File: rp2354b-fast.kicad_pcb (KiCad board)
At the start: 4 copper layers, 70 x 70 mm, 90 parts, among them J1 USB_C_Receptacle_USB2.0_16P, J2 TC2030-Tag, J3 Batt-Con, J4 MSD-10-C, J5 STPR_OUT, J6 Conn_01x03_Socket, SW1 BOOT, SW2 RUN, U1 RP2354B, U2 TPS63061, U3 USBLC6-2P6, U4 BMP581, U5 TLV75801PDRV, U6 TLV75533PDRV, U7 DRV8461SPWP, U8 ISM6HG256X, U9 MMC5983MA, Y1 12MHz

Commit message: v1.1c
sx1262 placement
need to route and assign pins
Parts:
- added C47: 100nF, Capacitor_SMD:C_0402_1005Metric, B.Cu at (127.5, 113.5)
- added C48: 10uF, Capacitor_SMD:C_0402_1005Metric, B.Cu at (125.6, 113.5)
- added U11: SX1262, WS-CORE-SX1262:CORE-1262, B.Cu at (118.4, 125.0)
- J4: value MSD-10-C -> CUI_MSD-10-C
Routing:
- net GND: track 56.5 -> 69.3 mm, vias 67 -> 73
- net +3V3: vias 35 -> 36

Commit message: sx1262 routes
routed!!
production ready??
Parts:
- J4: value CUI_MSD-10-C -> MSD-10-C
- moved R16 4.40 mm to (110.1, 104.4)
- moved R17 3.30 mm to (114.5, 104.4)
- moved R18 1.10 mm to (111.2, 104.4)
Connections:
- J4 pad 02: /GPIO14_CSN_SD -> /GPIO09_CSN_SD
- J4 pad 03: /GPIO19_SPI0_TX -> /GPIO11_SPI1_TX
- J4 pad 05: /GPIO18_SPI0_SCK -> /GPIO10_SPI1_SCK
- J4 pad 07: /GPIO16_SPI0_RX -> /GPIO08_SPI1_RX
- R15 pad 2: /GPIO16_SPI0_RX -> /GPIO08_SPI1_RX
- R16 pad 2: /GPIO18_SPI0_SCK -> /GPIO09_CSN_SD
- R17 pad 2: /GPIO19_SPI0_TX -> /GPIO10_SPI1_SCK
- R18 pad 2: /GPIO14_CSN_SD -> /GPIO11_SPI1_TX
- U1 pad 11: unconnected-(U1-GPIO12-Pad11) -> /GPIO12_CSN_RAD
- U1 pad 12: unconnected-(U1-GPIO13-Pad12) -> /GPIO13_DIO1_RAD
- U1 pad 13: unconnected-(U1-GPIO14-Pad13) -> /GPIO14_BUSY_RAD
- U1 pad 14: /GPIO14_CSN_SD -> /GPIO15_RESET_RAD
- U1 pad 6: unconnected-(U1-GPIO8-Pad6) -> /GPIO08_SPI1_RX
- U1 pad 7: unconnected-(U1-GPIO9-Pad7) -> /GPIO09_CSN_SD
- U1 pad 8: unconnected-(U1-GPIO10-Pad8) -> /GPIO10_SPI1_SCK
- U1 pad 9: unconnected-(U1-GPIO11-Pad9) -> /GPIO11_SPI1_TX
- U11 pad 14: unconnected-(U11-DIO1-Pad14) -> /GPIO13_DIO1_RAD
- U11 pad 3: unconnected-(U11-CS-Pad3) -> /GPIO12_CSN_RAD
- U11 pad 4: unconnected-(U11-CLK-Pad4) -> /GPIO10_SPI1_SCK
- U11 pad 5: unconnected-(U11-MOSI-Pad5) -> /GPIO11_SPI1_TX
- U11 pad 6: unconnected-(U11-MISO-Pad6) -> /GPIO08_SPI1_RX
- U11 pad 7: unconnected-(U11-RESET-Pad7) -> /GPIO15_RESET_RAD
- U11 pad 8: unconnected-(U11-BUSY-Pad8) -> /GPIO14_BUSY_RAD
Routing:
- net /GPIO10_SPI1_SCK: track 0.00 -> 70.0 mm, vias 0 -> 1
- net /GPIO08_SPI1_RX: track 0.00 -> 63.1 mm, vias 0 -> 1
- net /GPIO11_SPI1_TX: track 0.00 -> 58.7 mm, vias 0 -> 1
- net /GPIO12_CSN_RAD: track 0.00 -> 51.2 mm, vias 0 -> 1
- net /GPIO14_CSN_SD: track 48.2 -> 0.00 mm, vias 2 -> 0
- net /GPIO09_CSN_SD: track 0.00 -> 47.9 mm, vias 0 -> 2
- net /GPIO15_RESET_RAD: track 0.00 -> 43.4 mm, vias 0 -> 1
- net /GPIO14_BUSY_RAD: track 0.00 -> 38.9 mm, vias 0 -> 1
- net /GPIO18_SPI0_SCK: track 61.2 -> 23.5 mm, vias 2 -> 0
- net /GPIO19_SPI0_TX: track 52.7 -> 19.7 mm
- net /GPIO16_SPI0_RX: track 52.1 -> 21.5 mm
- net /GPIO13_DIO1_RAD: track 0.00 -> 29.2 mm, vias 0 -> 1
- net GND: track 69.3 -> 67.3 mm

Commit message: footprints
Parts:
- C1, C2: value 10pF -> TBA
- C11, C12, C13: footprint Capacitor_SMD:C_0402_1005Metric -> Capacitor_SMD:C_0603_1608Metric
- L1: footprint Inductor_SMD:L_0402_1005Metric -> Inductor_SMD:L_Coilcraft_XxL4020
- R11: value 1MR -> 100kR
- moved L1 9.28 mm to (134.6, 103.5), turned to 90 degrees
- moved C12 2.07 mm to (129.2, 104.5)
- moved C13 1.20 mm to (131.5, 105.3), turned to -90 degrees
- moved C11 0.73 mm to (129.2, 106.1)
- moved C10 0.43 mm to (128.9, 107.3)
- moved C9 0.20 mm to (120.7, 107.4)
- moved C7 0.16 mm to (129.4, 108.4)
- moved C8 0.10 mm to (122.2, 106.9)
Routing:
- net Net-(U2-L1): track 2.03 -> 13.6 mm
- net Net-(U2-L2): track 2.08 -> 10.3 mm
- net Net-(C11-Pad2): track 0.94 -> 2.24 mm
- net Net-(C12-Pad2): track 0.94 -> 1.51 mm
- net GND: track 67.3 -> 67.7 mm, vias 73 -> 76

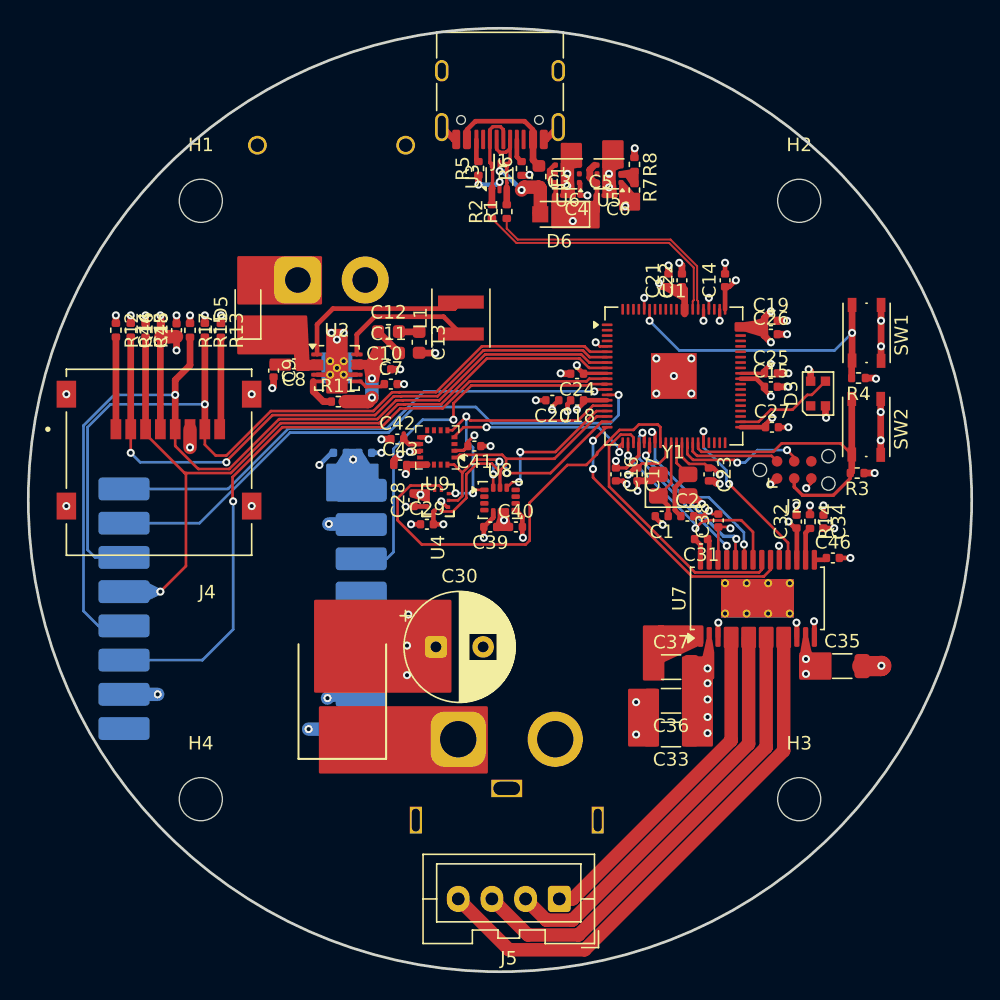
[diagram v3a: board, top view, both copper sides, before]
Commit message: v1.1e
added header pins for the driver and some extras for rbf and others.
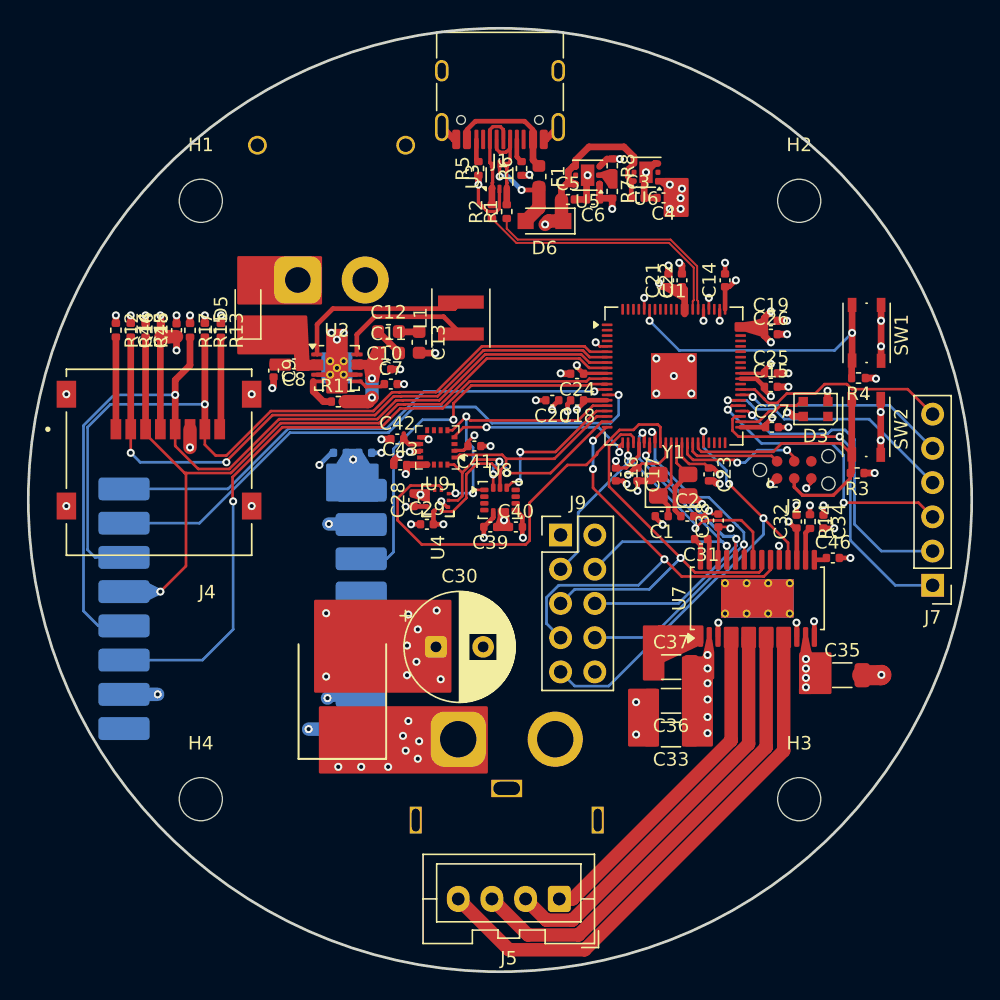
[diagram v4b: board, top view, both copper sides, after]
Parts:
- added J7: Conn_01x06, Connector_PinHeader_2.54mm:PinHeader_1x06_P2.54mm_Vertical, F.Cu at (169.6, 123.3)
- added J9: Conn_02x06_Odd_Even, Connector_PinHeader_2.54mm:PinHeader_2x05_P2.54mm_Vertical, F.Cu at (142.0, 119.6)
- C3, C4, C5, C6: footprint Capacitor_SMD:C_01005_0402Metric -> Capacitor_SMD:C_0402_1005Metric
- moved C4 6.45 mm to (149.6, 94.6)
- moved C3 5.84 mm to (147.7, 94.6)
- moved U6 5.83 mm to (148.3, 92.7)
- moved C5 2.45 mm to (142.5, 94.7)
- moved C6 1.89 mm to (144.4, 94.7)
- moved R8 1.65 mm to (145.8, 92.2)
- moved R7 1.65 mm to (145.8, 94.1)
- moved U5 1.59 mm to (144.0, 92.9)
- moved D6 1.20 mm to (140.8, 96.3)
- moved D3 1.16 mm to (160.9, 110.2), turned to 180 degrees
- moved C35 0.68 mm to (162.9, 130.0)
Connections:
- U1 pad 43: unconnected-(U1-GPIO34-Pad43) -> Net-(J7-Pin_1)
- U1 pad 44: unconnected-(U1-GPIO35-Pad44) -> Net-(J7-Pin_2)
- U1 pad 45: unconnected-(U1-GPIO36-Pad45) -> Net-(J7-Pin_3)
- U1 pad 46: unconnected-(U1-GPIO37-Pad46) -> Net-(J7-Pin_4)
- U1 pad 47: unconnected-(U1-GPIO38-Pad47) -> Net-(J7-Pin_5)
- U1 pad 48: unconnected-(U1-GPIO39-Pad48) -> Net-(J7-Pin_6)
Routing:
- net Net-(J7-Pin_1): track 0.00 -> 25.2 mm, vias 0 -> 1
- net Net-(J7-Pin_2): track 0.00 -> 22.5 mm, vias 0 -> 1
- net Net-(J7-Pin_3): track 0.00 -> 21.6 mm, vias 0 -> 2
- net /GPIO28_CSN_STPR: track 13.0 -> 34.3 mm, vias 2 -> 3
- net Net-(J7-Pin_4): track 0.00 -> 18.7 mm, vias 0 -> 1
- net Net-(J7-Pin_6): track 0.00 -> 16.2 mm
- net Net-(J7-Pin_5): track 0.00 -> 15.9 mm, vias 0 -> 1
- net /STPER_STEP: track 14.0 -> 28.0 mm
- net /GPIO20_SPI0_RX: track 21.5 -> 35.2 mm, vias 2 -> 3
- net /STPER_DIR: track 12.1 -> 24.9 mm
- net /STPER_ENABLE: track 13.1 -> 23.9 mm
- net /GPIO22_SPIO_SCK: track 15.4 -> 25.9 mm
- net /GPIO23_SPIO_TX: track 20.4 -> 30.7 mm, vias 0 -> 1
- net GND: track 67.7 -> 77.6 mm, vias 76 -> 73
- net /GPIO33_LED: track 7.55 -> 5.27 mm
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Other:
- board text added: "AIAA, CSU Fresno Airbrakes Controller V1.1e"
- board text removed: "AIAA, CSU Fresno Airbrakes Controller V1.1"

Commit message: hmm
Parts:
- moved J5 10.2 mm to (148.6, 138.8), turned to -90 degrees
- moved L1 9.22 mm to (125.4, 102.8), turned to 180 degrees
- moved J3 2.30 mm to (122.5, 98.4)
- moved D5 1.25 mm to (118.8, 101.5)
- moved J6 0.93 mm to (133.5, 135.0)
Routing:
- net /HV_16v8/BOUT1: track 40.2 -> 24.2 mm
- net /HV_16v8/BOUT2: track 35.4 -> 20.3 mm
- net Net-(U2-L1): track 13.6 -> 0.00 mm
- net /HV_16v8/AOUT2: track 30.5 -> 17.8 mm
- net Net-(U2-L2): track 10.3 -> 0.00 mm
- net /HV_16v8/AOUT1: track 25.3 -> 15.4 mm
- net GND: vias 73 -> 71

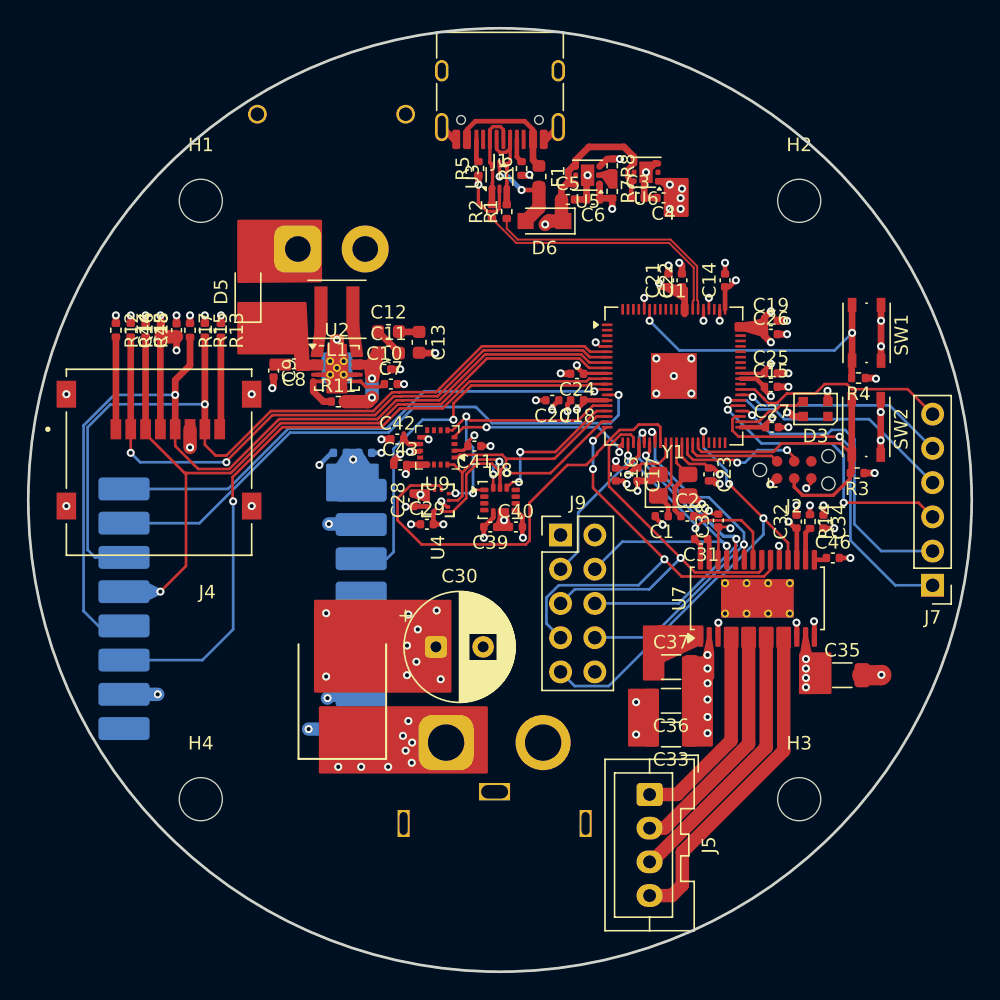
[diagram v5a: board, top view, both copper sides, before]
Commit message: v1.1e for real
ordered!
Redid high power side.
Added breakouts for power and the motor driver.
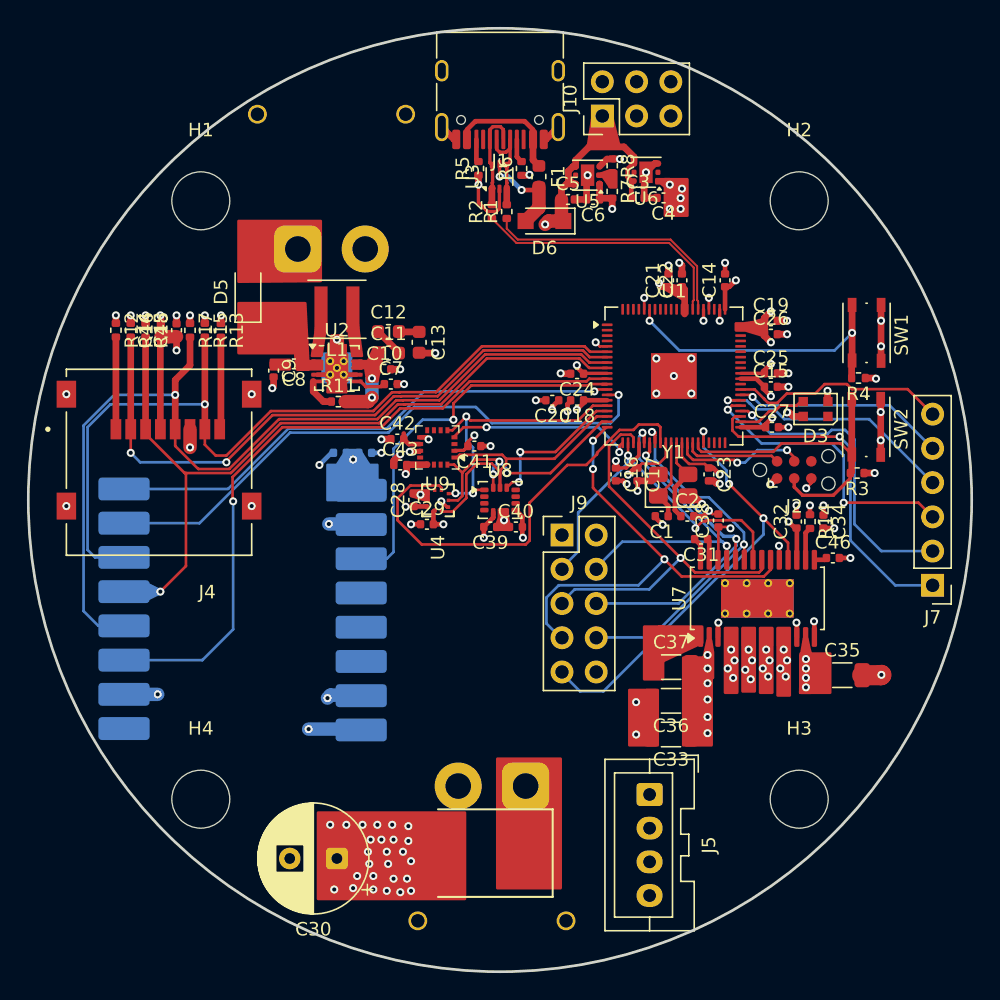
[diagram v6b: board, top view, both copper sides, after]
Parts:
- removed J6: Conn_01x03_Socket, Connector_AMASS:AMASS_XT60IPW-M_1x03_P7.20mm_Horizontal
- added J10: Power_Pins, Connector_PinHeader_2.54mm:PinHeader_2x03_P2.54mm_Vertical, F.Cu at (145.1, 88.5)
- added J8: Conn_01x02_Socket, Connector_AMASS:AMASS_XT30PW-M_1x02_P2.50mm_Horizontal, B.Cu at (139.4, 138.2)
- H1, H2, H3, H4: footprint MountingHole:MountingHole_3.2mm_M3 -> MountingHole:MountingHole_4.3mm_M4
- moved C30 17.3 mm to (125.4, 143.6), turned to 180 degrees
- moved D4 16.0 mm to (136.5, 143.2), turned to 180 degrees
- moved J9 0.11 mm to (142.1, 119.6)
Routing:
- net +DVDD: track 54.3 -> 69.0 mm
- net /HV_16v8/AOUT1: track 15.4 -> 13.9 mm, vias 0 -> 4
- net /HV_16v8/AOUT2: track 17.8 -> 16.5 mm, vias 0 -> 4
- net +3V3: track 65.1 -> 64.1 mm
- net /HV_16v8/BOUT2: track 20.3 -> 19.3 mm, vias 0 -> 4
- net /HV_16v8/BOUT1: track 24.2 -> 23.6 mm, vias 0 -> 4
- net Net-(J8-Pin_1): vias 8 -> 0
- net +16V8: vias 19 -> 36

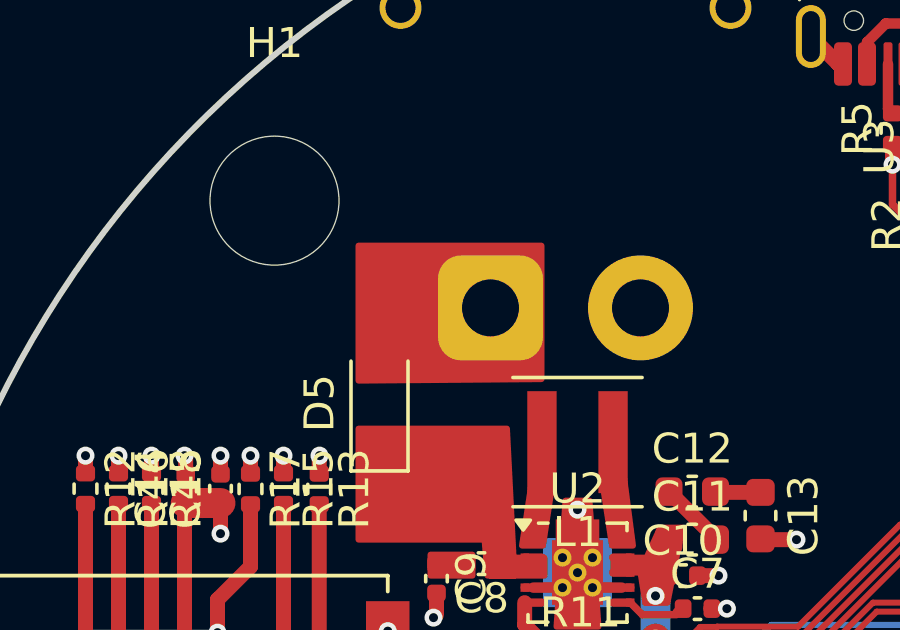
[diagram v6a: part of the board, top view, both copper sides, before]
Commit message: Changed Resistors
Changed many of the SD card resistors to 47kR.
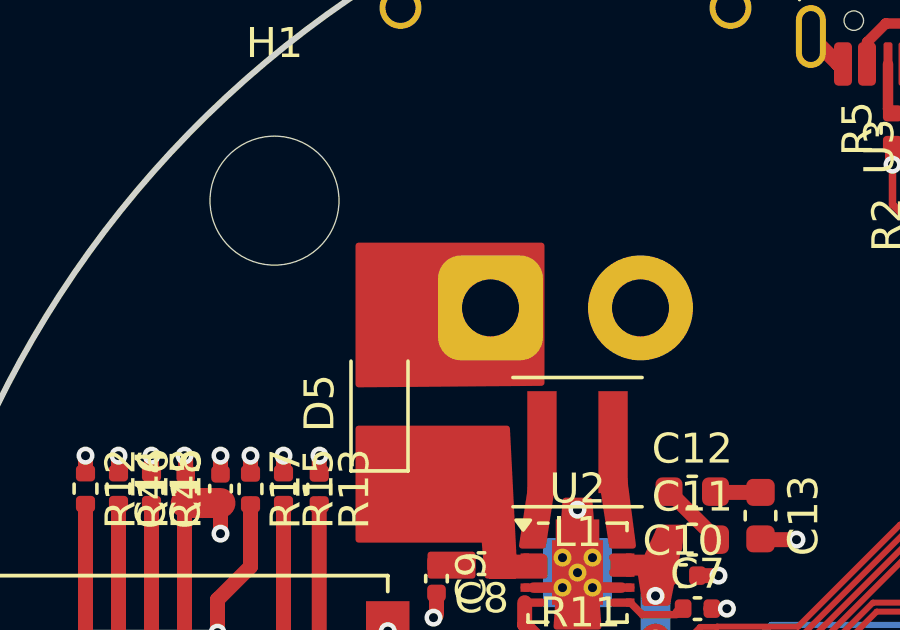
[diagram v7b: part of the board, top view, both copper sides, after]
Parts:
- R12, R13, R15, R16, R17, R18: value 10kR -> 47kR
- R3: value 10kR -> 4.7kR
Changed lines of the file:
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@@
 			)
 		)
-		(property "Value" "10kR"
+		(property "Value" "47kR"
 			(at -2.9 0.1 90)
 			(layer "F.Fab")
@@
 			)
 		)
-		(property "Value" "10kR"
+		(property "Value" "47kR"
 			(at -2.8 0 90)
 			(layer "F.Fab")
@@
 			)
 		)
-		(property "Value" "10kR"
+		(property "Value" "4.7kR"
 			(at 0 1.17 0)
 			(layer "F.Fab")
@@
 			)
 		)
-		(property "Value" "10kR"
+		(property "Value" "47kR"
 			(at -2.8 0.1 90)
 			(layer "F.Fab")
@@
 			)
 		)
-		(property "Value" "10kR"
+		(property "Value" "47kR"
 			(at -2.81 -0.01 90)
 			(layer "F.Fab")
@@
 			)
 		)
-		(property "Value" "10kR"
+		(property "Value" "47kR"
 			(at -2.71 0 90)
 			(layer "F.Fab")
@@
 			)
 		)
-		(property "Value" "10kR"
+		(property "Value" "47kR"
 			(at -2.8 0 90)
 			(layer "F.Fab")
@@
 	(gr_poly
 		(pts
-			(xy 124.2 100.75) (xy 118.1 100.8) (xy 118.1 96.3) (xy 124.2 96.3)
+			(xy 124.2 100.87459) (xy 118.1 100.92459) (xy 118.1 96.3) (xy 124.2 96.3)
 		)
 		(stroke
